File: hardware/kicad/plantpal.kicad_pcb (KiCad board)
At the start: 2 copper layers, 38.4 x 128.5 mm, 123 parts, among them J1 U262-161N-4BVC11, J2 +LIPO, J3 -LIPO, J4 687124182122, Q1 DMG1012UW, Q2 DMG3415U-7, Q3 MMBT3906, Q4 PMV32UP, Q5 DMG1012UW, Q6 AO3407A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

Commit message: wip
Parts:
- R12: value 2K -> 1K
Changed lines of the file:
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@@
     (tags "resistor")
     (property "Distributor" "LCSC")
-    (property "Distributor Link" "https://www.lcsc.com/product-detail/Chip-span-style-background-color-ff0-Resistor-span-Surface-Mount_UNI-ROYAL-Uniroyal-Elec-0402WGF2001TCE_C4109.html")
-    (property "Distributor Part Number" "C4109")
+    (property "Distributor Link" "https://www.lcsc.com/product-detail/Chip-Resistor-Surface-Mount_UNI-ROYAL-Uniroyal-Elec-0402WGF1001TCE_C11702.html")
+    (property "Distributor Part Number" "C11702")
     (property "Manufacturer" "UNI-ROYAL(Uniroyal Elec)")
-    (property "Manufacturer Part Number" "0402WGF2001TCE")
-    (property "Part Description" "Resistor 62.5mW ±1% 2kΩ ")
+    (property "Manufacturer Part Number" "0402WGF1001TCE")
+    (property "Part Description" "Resistor 62.5mW ±1% 1kΩ ")
     (property "Sheetfile" "usb_power.kicad_sch")
     (property "Sheetname" "USB Power")
@@
         (effects (font (size 0.3 0.3) (thickness 0.075)))
     )
-    (fp_text value "2K" (at 0.64 -0.55 90) (layer "F.Fab")
+    (fp_text value "1K" (at 0.64 -0.55 90) (layer "F.Fab")
         (effects (font (size 0.3 0.3) (thickness 0.075)))
     )

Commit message: change fpc connector
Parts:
- J4: value 687124182122 -> HC-FPC-05-09-24RLTAG; footprint plantpal:687124182122 -> plantpal:FPC-SMD_24P-P0.50_HC-FPC-05-09-24RLTAG
- turned J4 to 180 degrees

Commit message: add jst battery
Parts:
- added BT1: S2B-PH-SM4-TB(LF)(SN), plantpal:JST_PH_S2B-PH-SM4-TB_1x02-1MP_P2.00mm_Horizontal, B.Cu at (98.8, 94.0)
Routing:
- net Net-(BT1-+): track 13.1 -> 52.0 mm

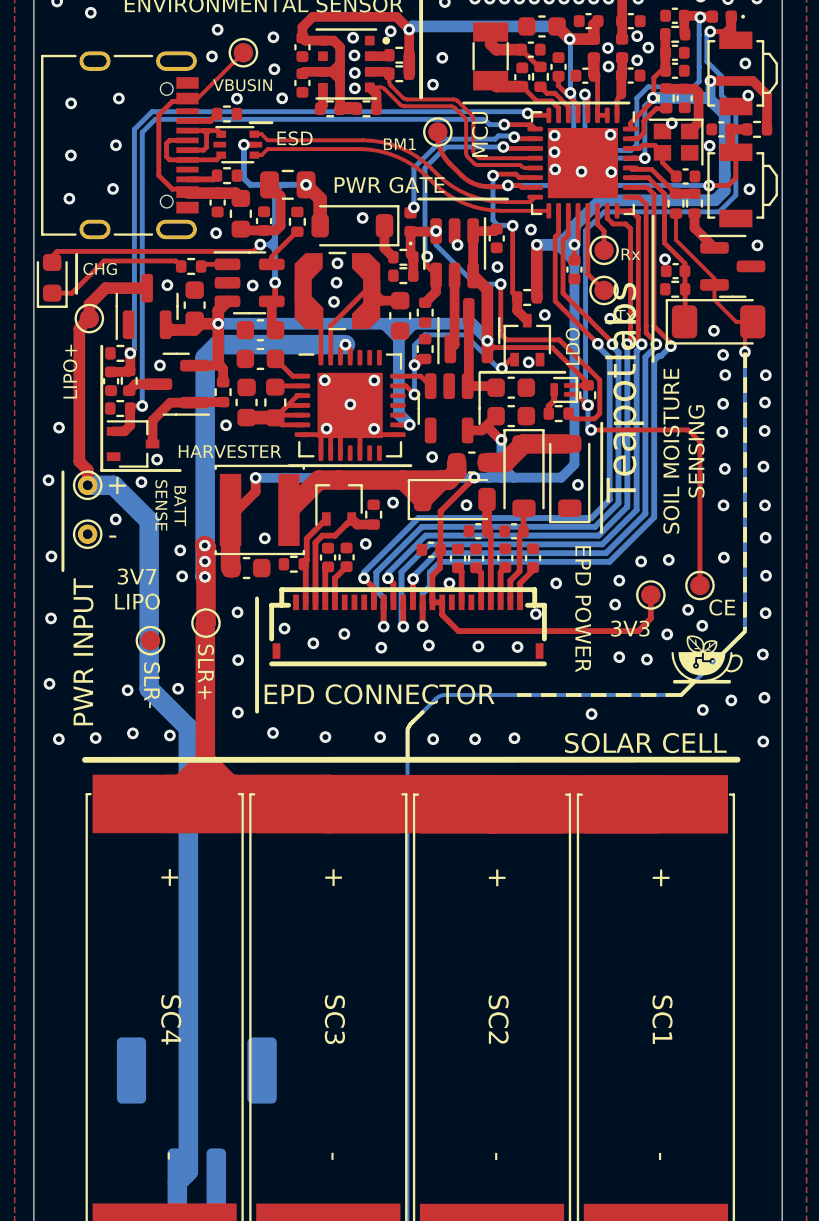
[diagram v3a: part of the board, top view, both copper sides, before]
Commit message: remove via in pad
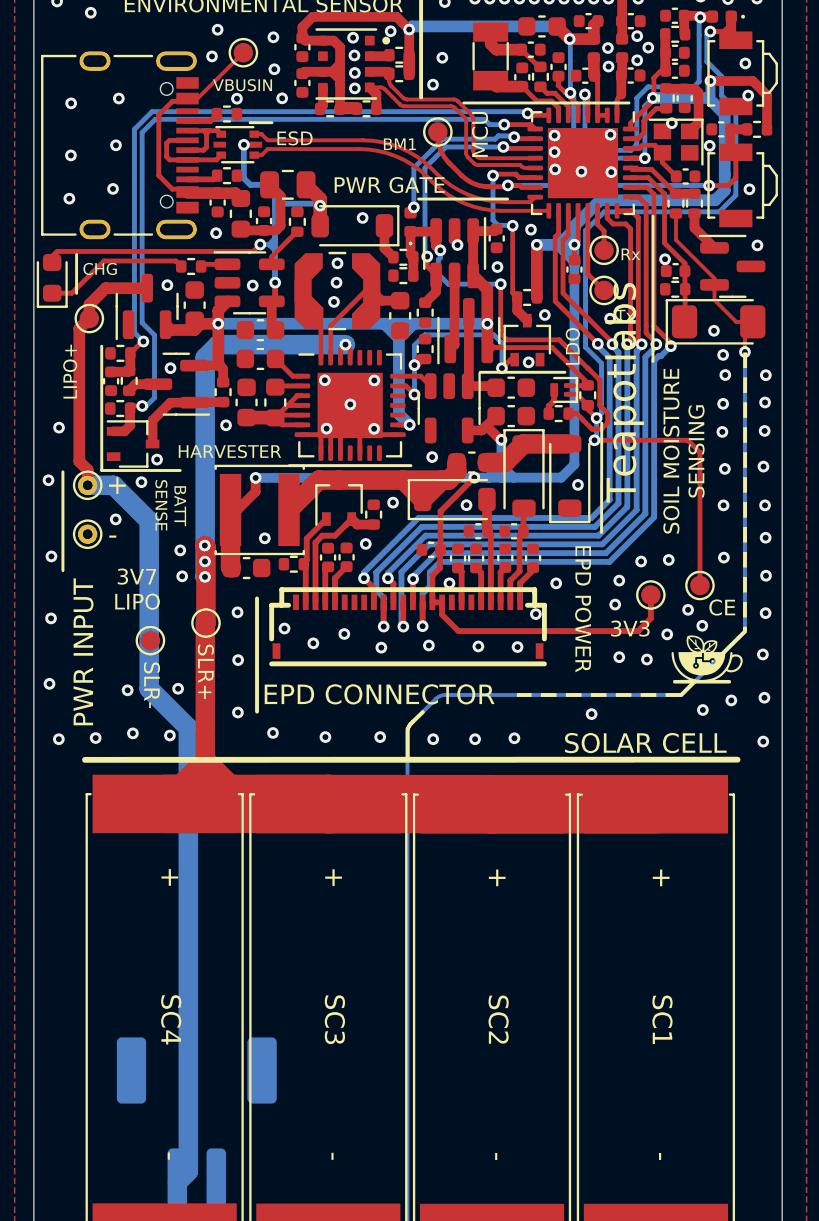
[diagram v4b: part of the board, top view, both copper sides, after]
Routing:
- net /Main Controller/M_DRV: track 20.7 -> 22.9 mm
- net /Main Controller/RESET_BTN: track 44.9 -> 46.0 mm
- net /Main Controller/PWR_STATUS: track 10.5 -> 11.3 mm
- net /Main Controller/BATT_MEAS_EN: track 37.2 -> 37.9 mm

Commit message: hardware/kicad/battery.kicad_sch
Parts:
- moved AE1 2.06 mm to (115.5, 34.4)
- moved C12 2.06 mm to (112.4, 34.4)
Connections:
- net Net-(AE1-FEED) renamed /Main Controller/ANT_FEED
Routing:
- net /Main Controller/ANT_FEED: track 4.52 -> 6.57 mm
- net GND: track 19.9 -> 20.9 mm
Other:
- board text added: "REVISION 2"
- board text removed: "REVISION 1"

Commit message: update incorrect D1 value
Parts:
- D1: value VLMO1500-GS08 -> VLMO1300-GS08
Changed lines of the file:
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@@
         (effects (font (size 0.3 0.3) (thickness 0.075)))
     )
-    (fp_text value "VLMO1500-GS08" (at 0 1.43 90) (layer "F.Fab")
+    (fp_text value "VLMO1300-GS08" (at 0 1.43 90) (layer "F.Fab")
         (effects (font (size 0.3 0.3) (thickness 0.075)))
     )

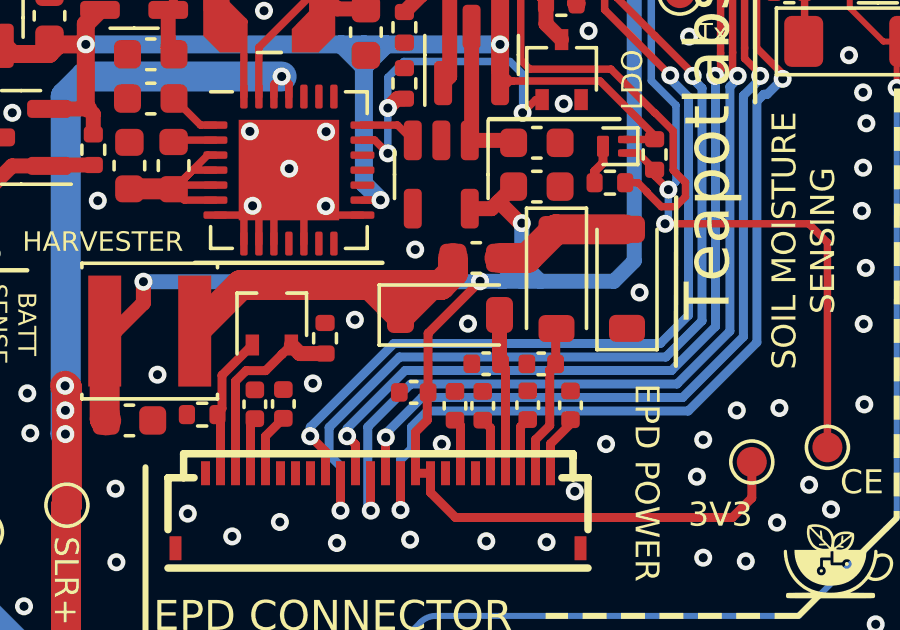
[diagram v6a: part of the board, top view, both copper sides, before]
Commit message: fix D6 polarity
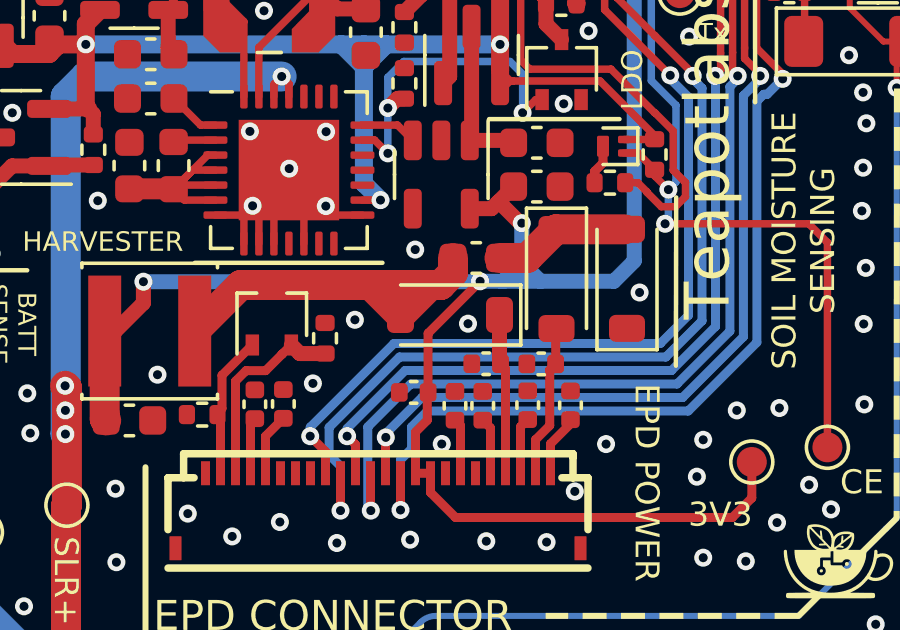
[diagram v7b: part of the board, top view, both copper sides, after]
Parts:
- turned D6 to 180 degrees
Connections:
- C40 pad 2: Net-(D6-K) -> Net-(D6-A)
- D6 pad 1: Net-(D6-K) -> /Display/PREVGH
- D6 pad 2: /Display/PREVGH -> Net-(D6-A)
- L5 pad 2: Net-(D6-K) -> Net-(D6-A)
- Q7 pad 3: Net-(D6-K) -> Net-(D6-A)
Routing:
- net Net-(D6-K): track 13.1 -> 0.00 mm
- net Net-(D6-A): track 0.00 -> 13.1 mm
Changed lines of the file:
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@@
   (net 30 "/Display/PREVGH")
   (net 31 "Net-(D4-K)")
-  (net 32 "Net-(D6-K)")
+  (net 32 "Net-(D6-A)")
   (net 33 "Net-(D1-K)")
   (net 34 "Net-(D2-K)")
@@
       (net 8 "+3V3") (pinfunction "1") (pintype "passive"))
     (pad "2" smd rect (at 1.5 0) (size 1.1 3.7) (layers "F.Cu" "F.Paste" "F.Mask")
-      (net 32 "Net-(D6-K)") (pinfunction "2") (pintype "passive"))
+      (net 32 "Net-(D6-A)") (pinfunction "2") (pintype "passive"))
     (model "${KIPRJMOD}/library/3dmodels/ASPI-4020S-120M-T.STEP"
       (offset (xyz 0 0 0))
@@
       (net 46 "/Display/RESE") (pinfunction "S") (pintype "passive"))
     (pad "3" smd rect (at 1 0) (size 0.45 0.7) (layers "F.Cu" "F.Paste" "F.Mask")
-      (net 32 "Net-(D6-K)") (pinfunction "D") (pintype "passive"))
+      (net 32 "Net-(D6-A)") (pinfunction "D") (pintype "passive"))
     (model "${KICAD6_3DMODEL_DIR}/Package_TO_SOT_SMD.3dshapes/SOT-323_SC-70.wrl"
       (offset (xyz 0 0 0))
@@
   )
   (footprint "Diode_SMD:D_SOD-123" (layer "F.Cu")
-    (at 112.08 61.84)
+    (at 112.08 61.84 180)
     (descr "SOD-123")
     (tags "SOD-123")
@@
     (fp_line (start 1.4 0.9) (end -1.4 0.9)
       (stroke (width 0.1) (type solid)) (layer "F.Fab"))
-    (pad "1" smd roundrect (at -1.65 0) (size 0.9 1.2) (layers "F.Cu" "F.Paste" "F.Mask") (roundrect_rratio 0.25)
-      (net 32 "Net-(D6-K)") (pinfunction "K") (pintype "passive"))
-    (pad "2" smd roundrect (at 1.65 0) (size 0.9 1.2) (layers "F.Cu" "F.Paste" "F.Mask") (roundrect_rratio 0.25)
-      (net 30 "/Display/PREVGH") (pinfunction "A") (pintype "passive"))
+    (pad "1" smd roundrect (at -1.65 0 180) (size 0.9 1.2) (layers "F.Cu" "F.Paste" "F.Mask") (roundrect_rratio 0.25)
+      (net 30 "/Display/PREVGH") (pinfunction "K") (pintype "passive"))
+    (pad "2" smd roundrect (at 1.65 0 180) (size 0.9 1.2) (layers "F.Cu" "F.Paste" "F.Mask") (roundrect_rratio 0.25)
+      (net 32 "Net-(D6-A)") (pinfunction "A") (pintype "passive"))
     (model "${KICAD6_3DMODEL_DIR}/Diode_SMD.3dshapes/D_SOD-123.wrl"
       (offset (xyz 0 0 0))
@@
     (tags "LED")
     (property "Distributor" "LCSC")
-    (property "Distributor Link" "https://www.lcsc.com/product-detail/Light-Emitting-Diodes-span-style-background-color-ff0-LED-span_Vishay-Intertech-VLMO1500-GS08_C3000857.html")
-    (property "Distributor Part Number" "C3000857")
+    (property "Distributor Link" "https://www.lcsc.com/product-detail/Light-Emitting-Diodes-LED_Vishay-Intertech-VLMO1300-GS08_C5184984.html")
+    (property "Distributor Part Number" "C5184984")
     (property "Manufacturer" "Vishay Intertech")
-    (property "Manufacturer Part Number" "VLMO1500-GS08")
+    (property "Manufacturer Part Number" "VLMO1300-GS08")
     (property "Part Description" "Orange 2V 20mA")
     (property "Sheetfile" "usb_power.kicad_sch")
@@
     (property "Sheetfile" "usb_power.kicad_sch")
     (property "Sheetname" "USB Power")
+    (property "ki_description" "Ferrite bead")
+    (property "ki_keywords" "L ferrite bead inductor filter")
     (attr smd)
     (fp_text reference "FB1" (at 1.1225 0.11 -180) (layer "F.Fab")
@@
       (net 31 "Net-(D4-K)") (pintype "passive"))
     (pad "2" smd roundrect (at 0.775 0 180) (size 0.9 0.95) (layers "F.Cu" "F.Paste" "F.Mask") (roundrect_rratio 0.25)
-      (net 32 "Net-(D6-K)") (pintype "passive"))
+      (net 32 "Net-(D6-A)") (pintype "passive"))
     (model "${KICAD6_3DMODEL_DIR}/Capacitor_SMD.3dshapes/C_0603_1608Metric.wrl"
       (offset (xyz 0 0 0))

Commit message: wip: removing powergate
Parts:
- removed C24: 100n, Capacitor_SMD:C_0402_1005Metric
- removed D2: B5819W, Diode_SMD:D_SOD-123
- removed D7, D8: RB161QS-40T18R, plantpal:D_0402_1005Metric
- removed Q2: DMG3415U-7, Package_TO_SOT_SMD:SOT-23
- removed Q8: PMZ350UPEYL, plantpal:SOT-883
- removed R14, R15: 16K9, Resistor_SMD:R_0402_1005Metric
- removed R27: 10K, Resistor_SMD:R_0402_1005Metric
- removed R28, R5: 1M, Resistor_SMD:R_0402_1005Metric
- removed U5: TPL5110, Package_TO_SOT_SMD:SOT-23-6
- moved G*** 29.1 mm to (108.1, 46.3)
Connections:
- net /Power Gate and Regulator/LDO_EN renamed /Power Regulator/LDO_EN
- C25 pad 1: Net-(Q2-D) -> +BATT
- SW2 pad 1: /Main Controller/RESET_BTN -> /Main Controller/CHIP_EN
- TP9 pad 1: /Main Controller/RESET_BTN -> /Main Controller/CHIP_EN
- U1 pad 10: /Main Controller/M_DRVOUT -> unconnected-(U1-MTMS/GPIO4/FSPIHD/ADC1_CH4-Pad10)
- U1 pad 11: /Main Controller/DONE -> unconnected-(U1-MTDI/GPIO5/FSPIWP/ADC1_CH5-Pad11)
- U6 pad 1: Net-(Q2-D) -> +BATT
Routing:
- net /Main Controller/RESET_BTN: track 46.0 -> 0.00 mm, vias 3 -> 0
- net /Main Controller/CHIP_EN: track 18.3 -> 62.6 mm, vias 2 -> 4
- net /Main Controller/M_DRV: track 22.9 -> 0.00 mm, vias 2 -> 0
- net /Main Controller/DONE: track 13.5 -> 0.00 mm, vias 2 -> 0
- net +BATT: track 46.0 -> 33.8 mm
- net /Main Controller/M_DRVOUT: track 9.33 -> 0.00 mm, vias 2 -> 0
- net Net-(Q2-D): track 5.30 -> 0.00 mm
- net /Power Gate and Regulator/DRV: track 3.86 -> 0.00 mm
- net /Main Controller/PWR_STATUS: track 11.3 -> 8.65 mm
- net Net-(D2-K): track 1.81 -> 0.00 mm
- net Net-(Q8-D): track 1.33 -> 0.00 mm
- net VBUS: track 30.1 -> 29.1 mm
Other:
- board text removed: "PWR GATE"
